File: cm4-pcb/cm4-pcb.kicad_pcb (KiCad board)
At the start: 2 copper layers, 140 x 70.5 mm, 37 parts, among them J1 Conn_01x02_Pin, J2 Conn_01x02_Pin, J3 USB1125-GF-B, J4 Conn_02x03_Odd_Even, J5 Conn_01x04, J6 J0011D21NL, J7 Conn_01x02, U1 Pfostenstecker_6_2x3, U2 Pfostenstecker_6_2x3, U3 TPD4EUSB30, U5 SMD-PUSH-BTN, U7 TPD4EUSB30

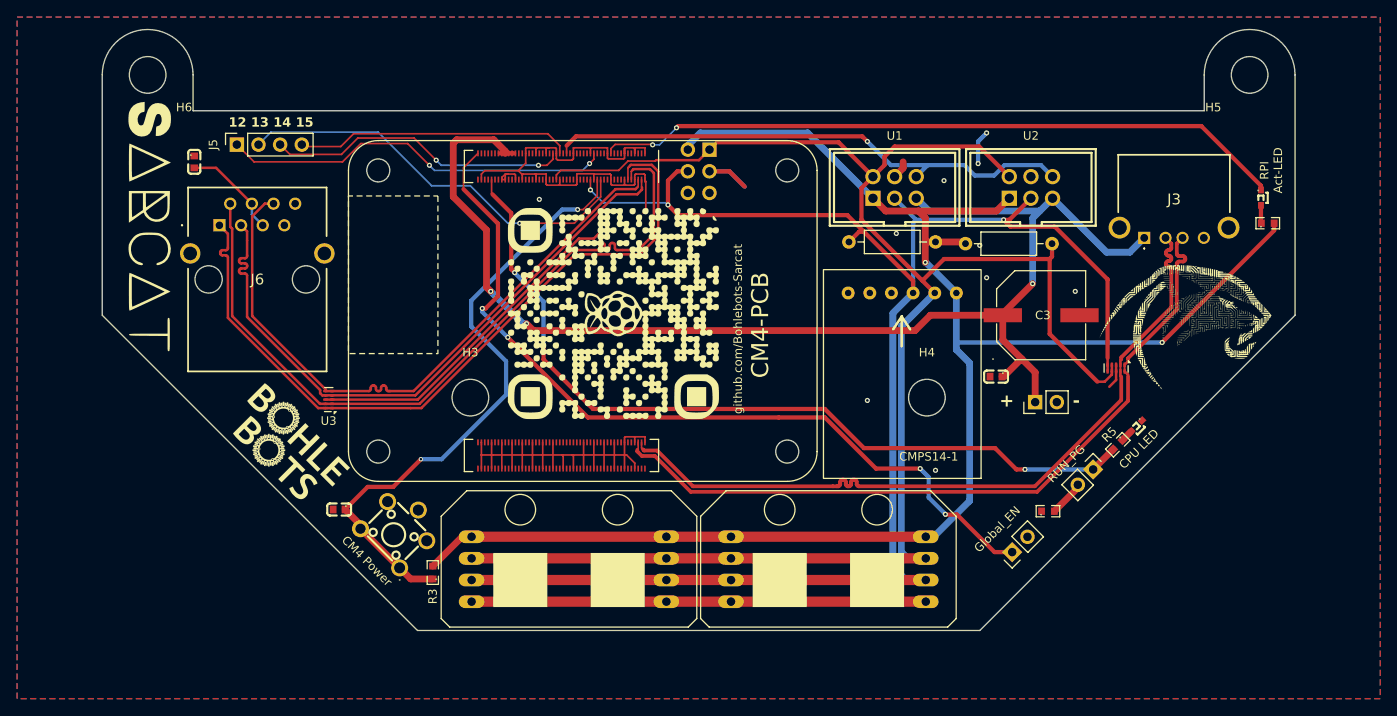
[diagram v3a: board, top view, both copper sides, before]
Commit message: Remove ESD Diodes
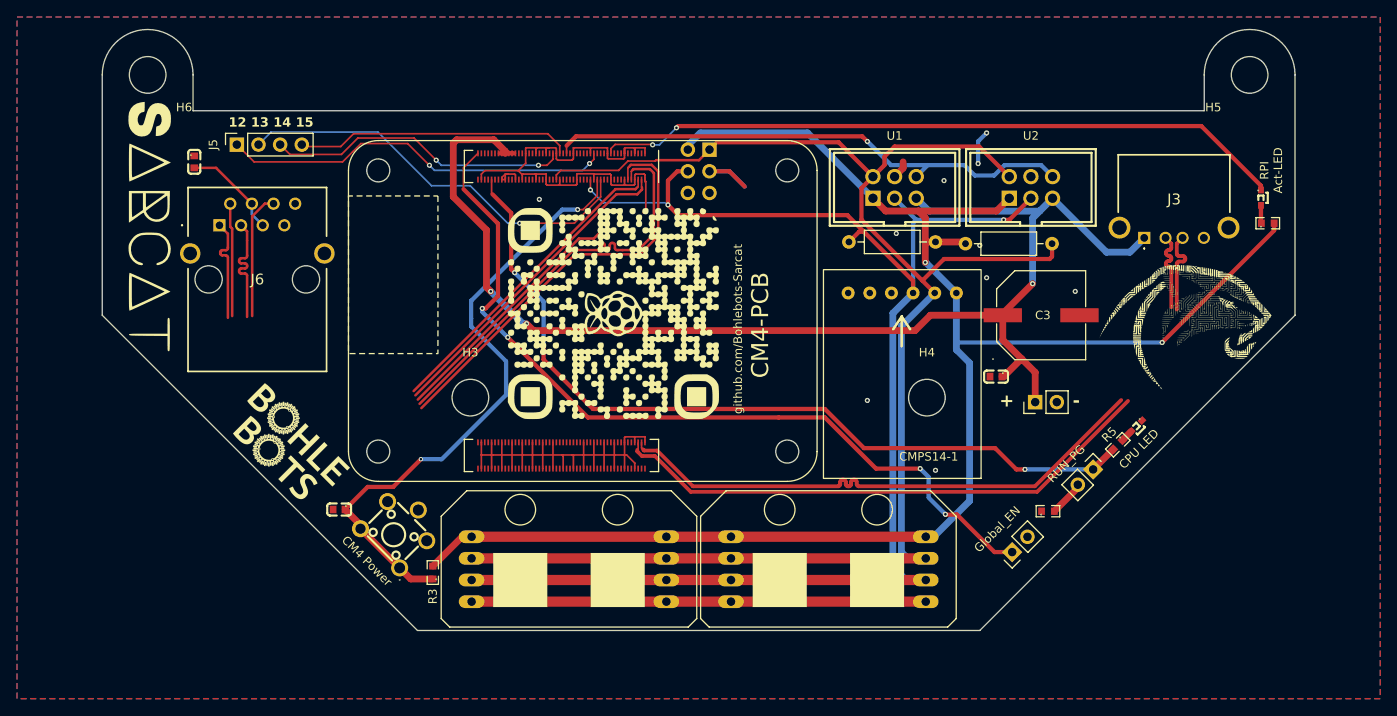
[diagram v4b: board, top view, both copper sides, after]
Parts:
- removed U3, U7: TPD4EUSB30, Package_SON:USON-10_2.5x1.0mm_P0.5mm
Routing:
- net /TRD0_P: track 88.9 -> 61.8 mm
- net /TRD0_N: track 88.8 -> 62.6 mm
- net SCL: track 196.5 -> 170.6 mm
- net /TRD1_N: track 76.3 -> 51.9 mm
- net /TRD1_P: track 75.5 -> 51.7 mm
- net SDA: track 204.6 -> 184.7 mm
- net GND: track 239.8 -> 226.1 mm
- net USB_D+: track 88.7 -> 75.3 mm
- net USB_D-: track 88.6 -> 75.2 mm

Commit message: Changed TVS Diodes
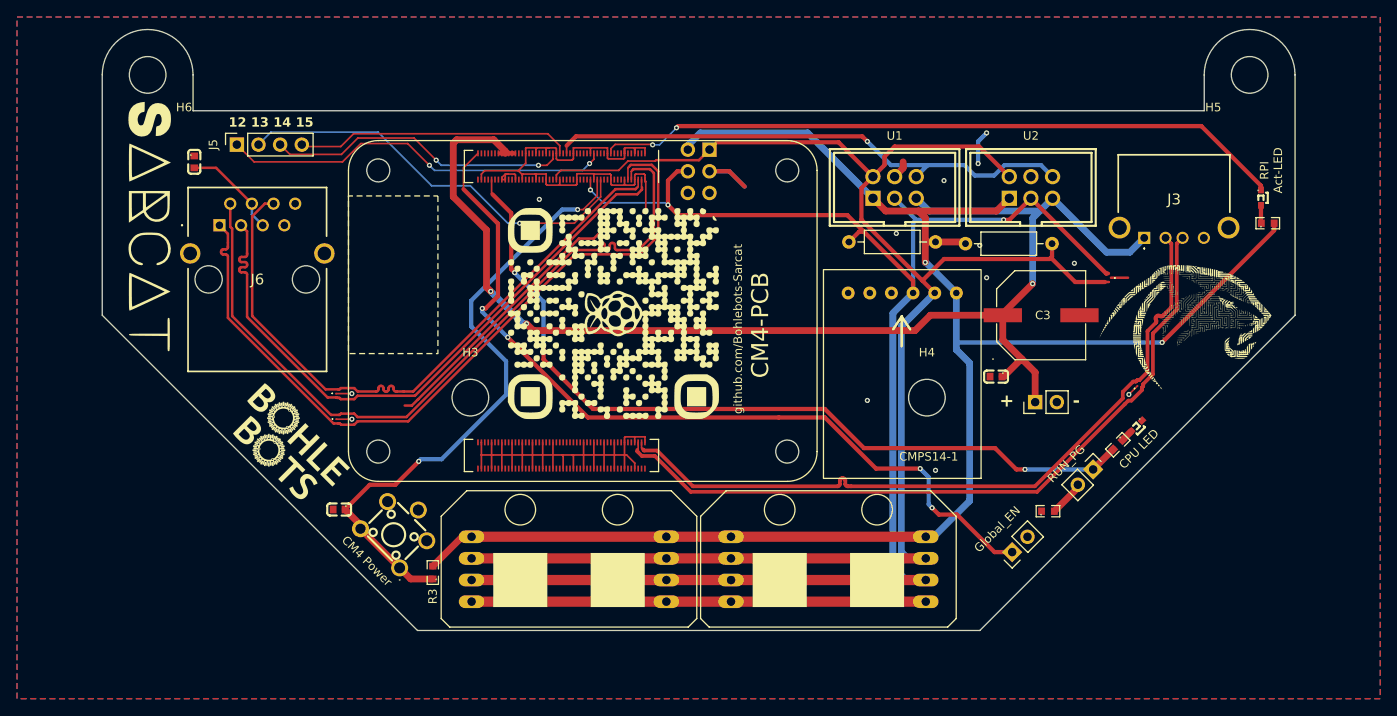
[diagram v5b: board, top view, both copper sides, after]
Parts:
- added D1: ESD122DMYR, ESD122DMYR:ESD122DMYR, F.Cu at (-42.4, 67.2)
- added D2: ESD122DMYR, ESD122DMYR:ESD122DMYR, F.Cu at (-42.4, 64.2)
- added D3: ESD122DMYR, ESD122DMYR:ESD122DMYR, F.Cu at (51.6, 63.2)
- added D4: ESD122DMYR, ESD122DMYR:ESD122DMYR, F.Cu at (48.3, 50.6)
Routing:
- net /TRD0_P: track 61.8 -> 90.3 mm
- net /TRD0_N: track 62.6 -> 90.2 mm
- net /TRD1_N: track 51.9 -> 76.3 mm
- net /TRD1_P: track 51.7 -> 75.5 mm
- net SCL: track 170.6 -> 183.4 mm
- net USB_D-: track 75.2 -> 87.0 mm
- net USB_D+: track 75.3 -> 87.1 mm
- net GND: track 226.1 -> 235.0 mm, vias 12 -> 15
- net SDA: track 184.7 -> 192.8 mm

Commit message: Added extra gnd zones to ensure right impendance for USB+Ethernet
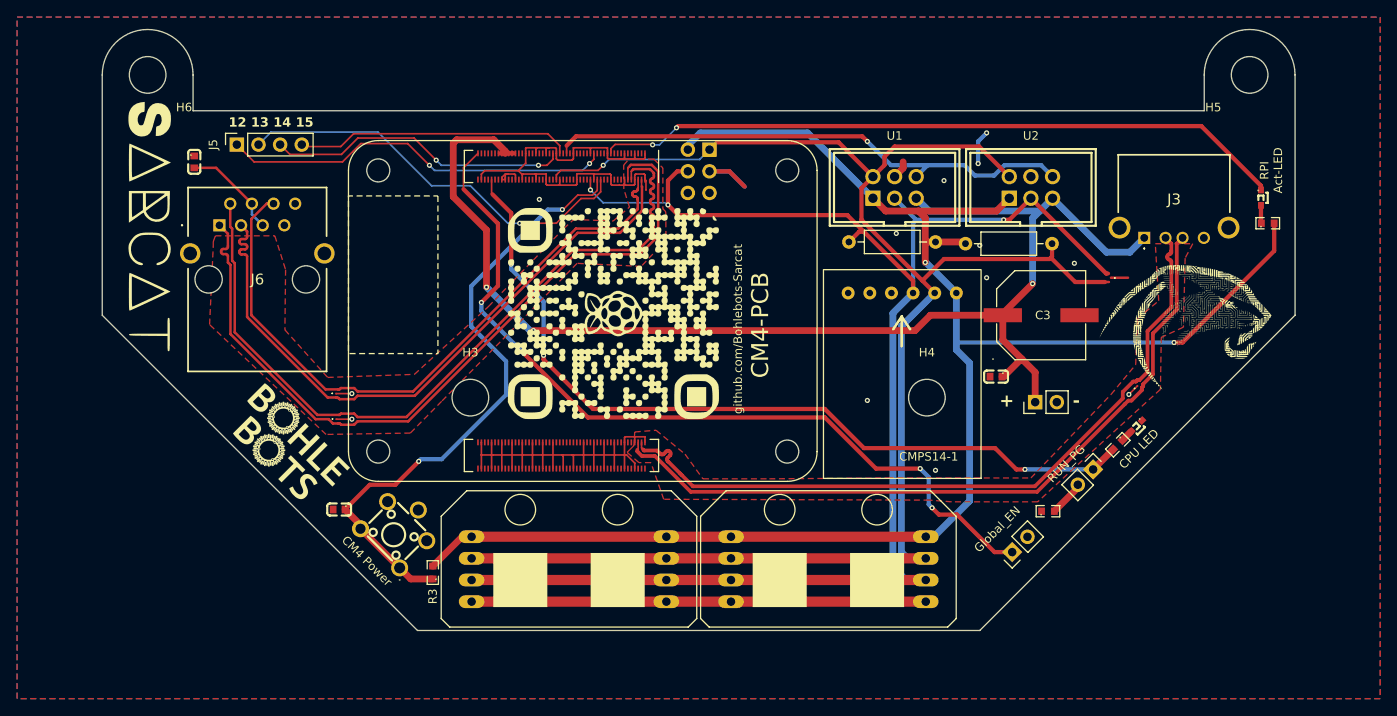
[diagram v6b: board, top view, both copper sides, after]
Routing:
- net GND: track 235.0 -> 199.9 mm, vias 15 -> 13
- net /TRD1_P: track 75.5 -> 76.9 mm
- net +3.3V: track 194.5 -> 195.9 mm
- net /TRD0_P: track 90.3 -> 91.2 mm
- net /TRD0_N: track 90.2 -> 91.1 mm
- net /TRD1_N: track 76.3 -> 77.0 mm
- net SHUTDOWN: track 72.9 -> 73.6 mm
- net SDA: track 192.8 -> 192.6 mm, vias 0 -> 1

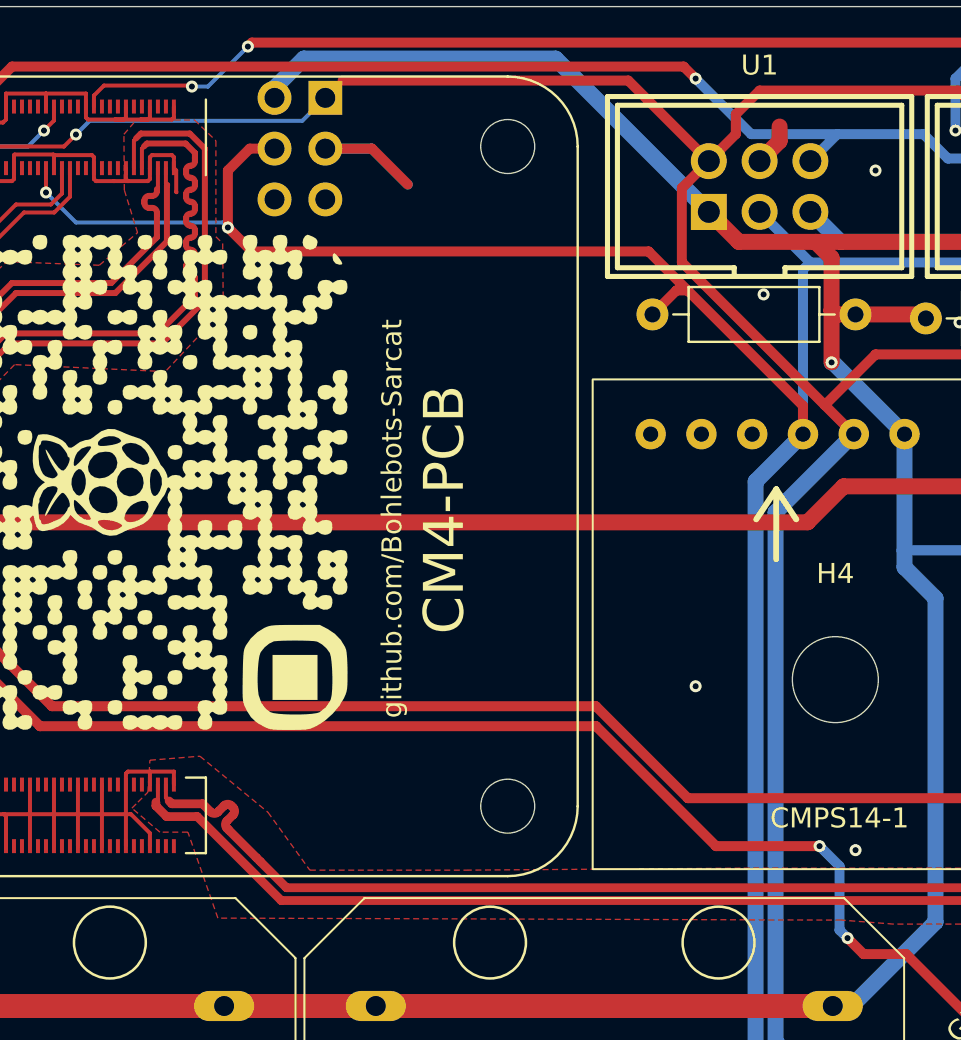
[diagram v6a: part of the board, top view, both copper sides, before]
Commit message: Modified GND zones
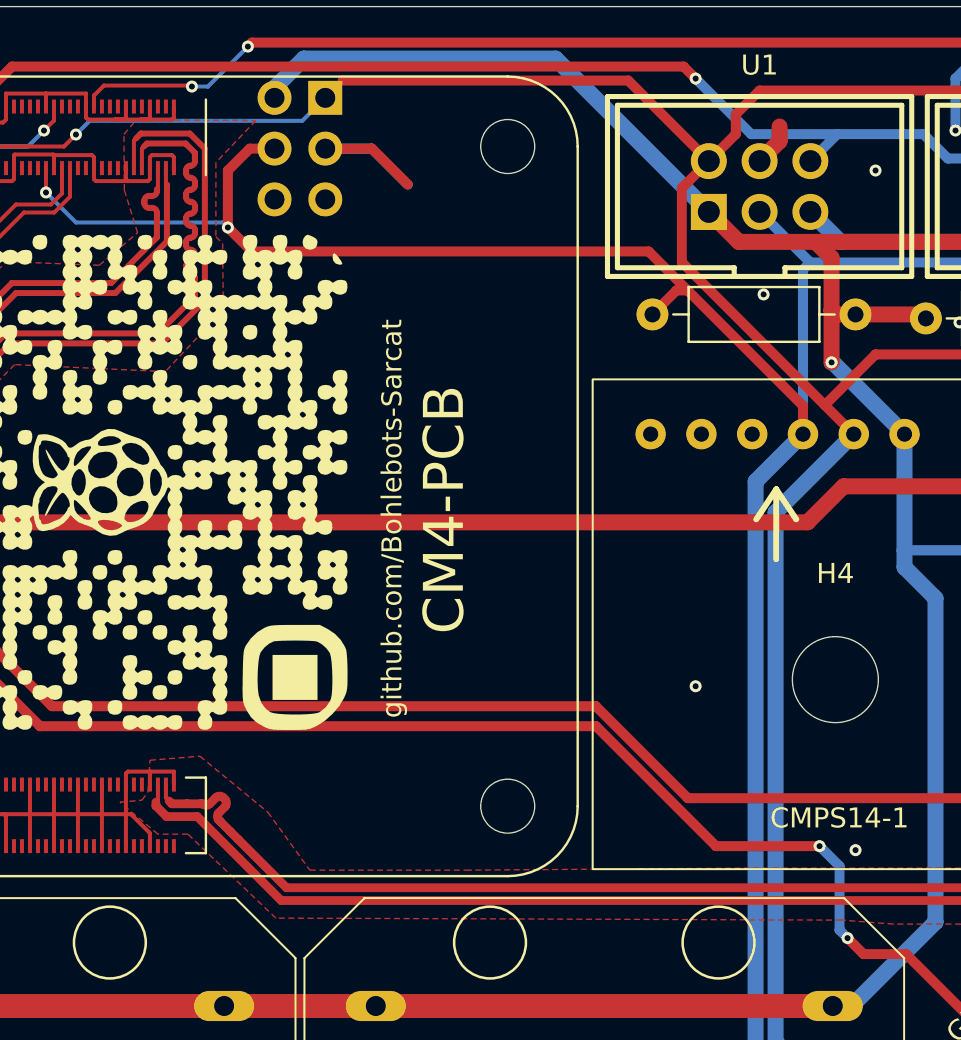
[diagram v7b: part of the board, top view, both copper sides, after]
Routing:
- net GND: track 199.9 -> 198.6 mm
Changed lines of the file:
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@@
 	)
 	(segment
-		(start -6.3 39.08)
-		(end -6.185 39.195)
-		(width 0.2)
-		(layer "F.Cu")
-		(net 1)
-	)
-	(segment
 		(start -20.7 69.92)
 		(end -20.7 71.4)
@@
 	)
 	(segment
-		(start -6.185 40.275)
-		(end -6.17 40.29)
-		(width 0.2)
-		(layer "F.Cu")
-		(net 1)
-	)
-	(segment
 		(start -14.8 71.4)
 		(end -13.5 71.4)
@@
 	)
 	(segment
-		(start -6.185 39.195)
-		(end -6.185 40.275)
-		(width 0.2)
-		(layer "F.Cu")
-		(net 1)
-	)
-	(segment
 		(start -9.24 36.65)
 		(end -10.6 36.65)
@@
 	)
 	(segment
-		(start -1.973725 73.773725)
-		(end -0.66745 75.08)
+		(start 52.68 61.667453)
+		(end 52.68 56.86745)
 		(width 0.44)
 		(layer "F.Cu")
@@
 	)
 	(segment
-		(start 52.68 61.667453)
-		(end 52.68 56.86745)
+		(start -4.95 70.88)
+		(end -4.86745 70.88)
 		(width 0.44)
 		(layer "F.Cu")
@@
 	)
 	(segment
-		(start -3.555309 72.192142)
-		(end -2.162307 73.585143)
+		(start 51.727783 62.61967)
+		(end 52.68 61.667453)
 		(width 0.44)
 		(layer "F.Cu")
@@
 	)
 	(segment
-		(start 51.727783 62.61967)
-		(end 52.68 61.667453)
+		(start -6.54 70.74)
+		(end -6.4 70.88)
 		(width 0.44)
 		(layer "F.Cu")
@@
 	)
 	(segment
-		(start -3.337394 71.431166)
-		(end -3.645822 71.739594)
+		(start -5.64 70.88)
+		(end -4.95 70.88)
 		(width 0.44)
 		(layer "F.Cu")
@@
 	)
 	(segment
-		(start -6.7 70.58)
-		(end -6.54 70.74)
-		(width 0.2)
+		(start -3.474449 72.273001)
+		(end -3.073725 72.673725)
+		(width 0.44)
 		(layer "F.Cu")
 		(net 115)
 	)
 	(segment
-		(start -3.645822 72.101632)
-		(end -3.555309 72.192142)
+		(start -3.073725 72.673725)
+		(end -0.66745 75.08)
 		(width 0.44)
 		(layer "F.Cu")
@@
 	)
 	(segment
-		(start 39.46745 75.08)
-		(end 49.78 64.76745)
+		(start -0.66745 75.08)
+		(end 39.46745 75.08)
 		(width 0.44)
 		(layer "F.Cu")
@@
 	)
 	(segment
+		(start -6.7 70.58)
+		(end -6.54 70.74)
+		(width 0.2)
+		(layer "F.Cu")
+		(net 115)
+	)
+	(segment
 		(start 55.48 46.597)
 		(end 55.235862 46.352862)
@@
 	)
 	(segment
-		(start -4.098368 71.287044)
-		(end -3.789941 70.978617)
+		(start 49.78 64.001766)
+		(end 51.001766 62.78)
 		(width 0.44)
 		(layer "F.Cu")
@@
 	)
 	(segment
-		(start 51.323223 62.76967)
-		(end 51.473223 62.61967)
+		(start -3.962353 71.785098)
+		(end -3.474449 72.273001)
 		(width 0.44)
 		(layer "F.Cu")
@@
 	)
 	(segment
-		(start -2.162307 73.585143)
-		(end -1.973725 73.773725)
+		(start 51.323223 62.76967)
+		(end 51.473223 62.61967)
 		(width 0.44)
 		(layer "F.Cu")
@@
 	)
 	(segment
-		(start 51.001766 62.78)
-		(end 51.312893 62.78)
+		(start -4.052866 71.694588)
+		(end -3.962353 71.785098)
 		(width 0.44)
 		(layer "F.Cu")
@@
 	)
 	(segment
-		(start -4.86745 70.88)
-		(end -4.460406 71.287044)
+		(start 51.473223 62.61967)
+		(end 51.727783 62.61967)
 		(width 0.44)
 		(layer "F.Cu")
@@
 	)
 	(segment
-		(start 51.473223 62.61967)
-		(end 51.727783 62.61967)
-		(width 0.44)
-		(layer "F.Cu")
-		(net 115)
-	)
-	(segment
-		(start 51.312893 62.78)
-		(end 51.323223 62.76967)
+		(start -3.744438 71.024122)
+		(end -4.052866 71.33255)
 		(width 0.44)
 		(layer "F.Cu")
@@
 	)
 	(segment
-		(start -3.427903 70.978617)
-		(end -3.337393 71.069128)
+		(start 39.46745 75.08)
+		(end 49.78 64.76745)
 		(width 0.44)
 		(layer "F.Cu")
@@
 	)
 	(segment
-		(start 49.78 64.001766)
-		(end 51.001766 62.78)
+		(start -6.4 70.88)
+		(end -5.64 70.88)
 		(width 0.44)
 		(layer "F.Cu")
@@
 	)
 	(segment
-		(start -0.66745 75.08)
-		(end 39.46745 75.08)
+		(start 51.312893 62.78)
+		(end 51.323223 62.76967)
 		(width 0.44)
 		(layer "F.Cu")
@@
 	)
 	(segment
-		(start -6.4 70.88)
-		(end -4.86745 70.88)
+		(start -3.834947 70.571573)
+		(end -3.744437 70.662084)
+		(width 0.44)
+		(layer "F.Cu")
+		(net 115)
+	)
+	(segment
+		(start 51.001766 62.78)
+		(end 51.312893 62.78)
 		(width 0.44)
 		(layer "F.Cu")
@@
 	)
 	(segment
-		(start 52.68 56.86745)
-		(end 55.48 54.06745)
+		(start -4.505412 70.88)
+		(end -4.196985 70.571573)
 		(width 0.44)
 		(layer "F.Cu")
@@
 	)
 	(segment
-		(start -6.54 70.74)
-		(end -6.4 70.88)
+		(start 52.68 56.86745)
+		(end 55.48 54.06745)
 		(width 0.44)
 		(layer "F.Cu")
@@
 	)
 	(arc
-		(start -3.645822 71.739594)
-		(mid -3.720803 71.920613)
-		(end -3.645822 72.101632)
+		(start -4.052866 71.33255)
+		(mid -4.127847 71.513569)
+		(end -4.052866 71.694588)
 		(width 0.44)
 		(layer "F.Cu")
@@
 	)
 	(arc
-		(start -4.460406 71.287044)
-		(mid -4.279387 71.362025)
-		(end -4.098368 71.287044)
+		(start 55.01555 48.07)
+		(mid 55.083567 47.905792)
+		(end 55.247775 47.837775)
 		(width 0.44)
 		(layer "F.Cu")
@@
 	)
 	(arc
-		(start 55.01555 48.07)
-		(mid 55.083567 47.905792)
-		(end 55.247775 47.837775)
+		(start -4.86745 70.88)
+		(mid -4.686431 70.954981)
+		(end -4.505412 70.88)
 		(width 0.44)
 		(layer "F.Cu")
@@
 	)
 	(arc
-		(start -3.789941 70.978617)
-		(mid -3.608922 70.903636)
-		(end -3.427903 70.978617)
+		(start -4.196985 70.571573)
+		(mid -4.015966 70.496592)
+		(end -3.834947 70.571573)
 		(width 0.44)
 		(layer "F.Cu")
@@
 	)
 	(arc
-		(start -3.337393 71.069128)
-		(mid -3.262413 71.250147)
-		(end -3.337394 71.431166)
+		(start 55.48 48.71)
+		(mid 55.411983 48.545792)
+		(end 55.247775 48.477775)
 		(width 0.44)
 		(layer "F.Cu")
@@
 	)
 	(arc
-		(start 55.48 48.71)
-		(mid 55.411983 48.545792)
-		(end 55.247775 48.477775)
+		(start -3.744437 70.662084)
+		(mid -3.669457 70.843103)
+		(end -3.744438 71.024122)
 		(width 0.44)
 		(layer "F.Cu")
@@
 			(pts
 				(xy 53.6 46.6) (xy 58 46.6) (xy 57.1 48.3) (xy 56.9 56.4) (xy 54.3 57.6) (xy 54.2 63.7) (xy 44.1 72.9)
-				(xy 39.8 76.9) (xy 29.7 76.9) (xy 27.1 76.7) (xy -4.1 76.6) (xy -5.6 72.3) (xy -7 72.3) (xy -8.4 71.1)
-				(xy -8.1 70.8) (xy -7.6 70.3) (xy -7.5 68.7) (xy -5 68.5) (xy -1.6 71.3) (xy 0.5 74.2) (xy 8.3 74.2)
+				(xy 39.8 76.9) (xy 29.7 76.9) (xy 27.1 76.7) (xy -1.2 76.6) (xy -5.6 72.4) (xy -7.1 72.4) (xy -9 70.8)
+				(xy -7.9 70.7) (xy -7.6 70.3) (xy -7.5 68.7) (xy -5 68.5) (xy -1.6 71.3) (xy 0.5 74.2) (xy 8.3 74.2)
 				(xy 22.2 74.1) (xy 39 74.1) (xy 48.4 64.3) (xy 51.3 60.8) (xy 51.5 55.4) (xy 54 53.3)
 			)
@@
 		(polygon
 			(pts
-				(xy -8.8 37.39) (xy -8.19 36.68) (xy -5.27 36.67) (xy -4.2 37.71) (xy -4.2 42.51) (xy -3.86 42.85)
+				(xy -8.8 37.39) (xy -8.19 36.68) (xy -2.2 36.7) (xy -4.2 38.8) (xy -4.2 42.51) (xy -3.86 42.85)
 				(xy -3.83 46.17) (xy -6.73 49.26) (xy -14.27 48.91) (xy -20.91 55.72) (xy -30.16 65.1) (xy -33.84 68.83)
 				(xy -43.73 68.99) (xy -57.4 56.1) (xy -56.97 46.91) (xy -56.97 46.37) (xy -56.72 45.68) (xy -49.743291 45.676431)
@@
 		(base_line
 			(pts
-				(xy -4.460406 71.287044) (xy -1.973725 73.773725)
+				(xy -5.64 70.88) (xy -4.86745 70.88) (xy -3.073725 72.673725)
 			)
 		)
@@
 		(corner_radius_percent 80)
 		(end
-			(xy -1.973725 73.773725)
+			(xy -3.073725 72.673725)
 		)
 		(initial_side "left")
 		(last_diff_pair_gap 0.18)
 		(last_netname "USB_D-")
-		(last_status "tuned")
+		(last_status "too_short")
 		(last_track_width 0.44)
-		(last_tuning "-0.0000 mm (tuned)")
+		(last_tuning "-0.0000 mm (too short)")
 		(max_amplitude 1)
 		(min_amplitude 0.2)
 		(min_spacing 0.6)
 		(origin
-			(xy -4.460406 71.287044)
+			(xy -5.64 70.88)
 		)
 		(override_custom_rules no)
@@
 		(target_length_min 999999.9)
 		(target_skew 0)
-		(target_skew_max 0.1)
-		(target_skew_min -0.1)
+		(target_skew_max 2147.483647)
+		(target_skew_min 0)
 		(tuning_mode "diff_pair_skew")
-		(members 199dcf3e-48b1-4650-847b-462838d3f6cb 2baf14bd-cf9b-4053-b2ea-effb7097463c
-			2d20994c-5b83-436b-b0dc-04fa2a71a772 369ff315-969e-4e2e-95e7-69485efaa84a
-			4c67aaf5-3f01-44f3-9ba9-f3d9367e8f94 510f94e8-b90c-4cd2-ba43-8e66cc711b1c
-			63fe0141-a6f3-49e2-93aa-45521757d3fc 84664819-e95b-41b8-9468-e783b4ddeeb4
-			99d705e5-1227-460b-95fa-d3ac59307f9e a3351e54-fe85-4e1c-89e8-e758bbec91fb
+		(members 17da5811-3e1d-4868-af66-e975795aa191 292b0936-4d61-42cb-b3f8-4e1e1361108f
+			3887bb07-3427-44ea-8385-99d94221428a 48e9511b-7bec-41cd-9749-64409c060476
+			55cb3e28-6c8c-40cf-a8de-f7c338ff634d 5b051c09-f18e-4edf-a1f0-a3c06ebfbc58
+			621e6ab0-e12b-42b6-a0e1-430657a8ef3a 6e2fc2df-8450-490d-9e8e-677f05a05981
+			7bc8341b-aa67-4268-8e71-fe0b17679e24 dc5742d0-5544-494d-9ec2-ca629fd63dc8
+			df139ad2-43c4-4b69-bcfb-d4ff8afacfb2 f9e02a09-ccc7-4eee-82c9-29ced5072af6
 		)
 	)
